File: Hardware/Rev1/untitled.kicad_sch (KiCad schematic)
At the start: 40 parts, among them J4 Female Conn, U3 TPS2596, U4 MCP2542FD-E/SN, U5 AZ1117-5.0, U6 AZ1117-5.0, U7 AZ1117IH-3.3, U9 TPS2596

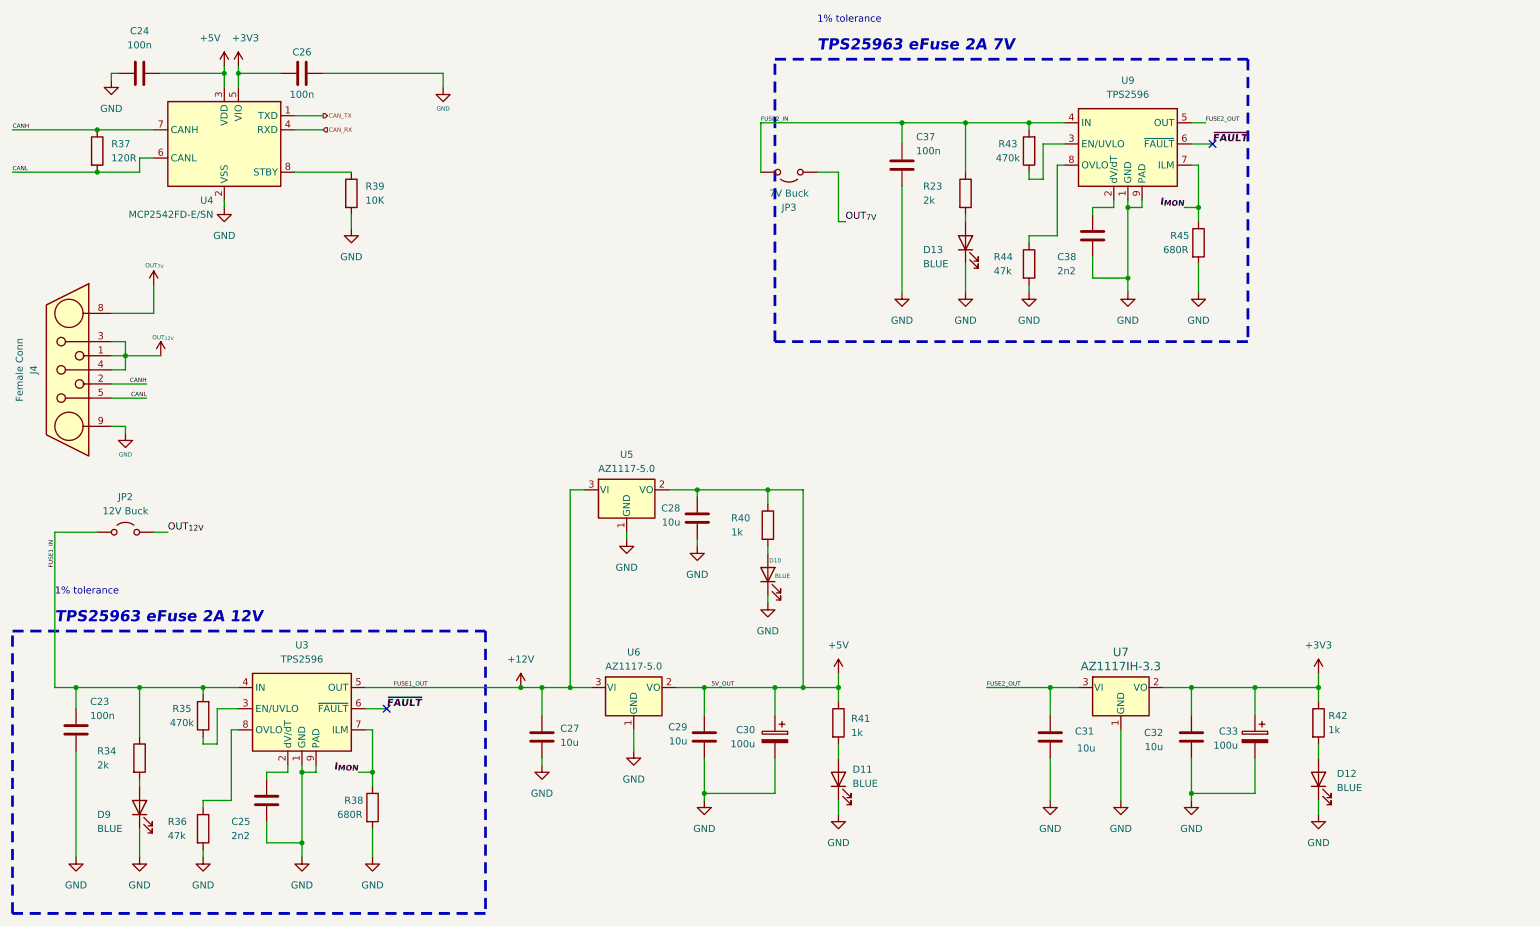
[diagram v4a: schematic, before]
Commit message: updated layout
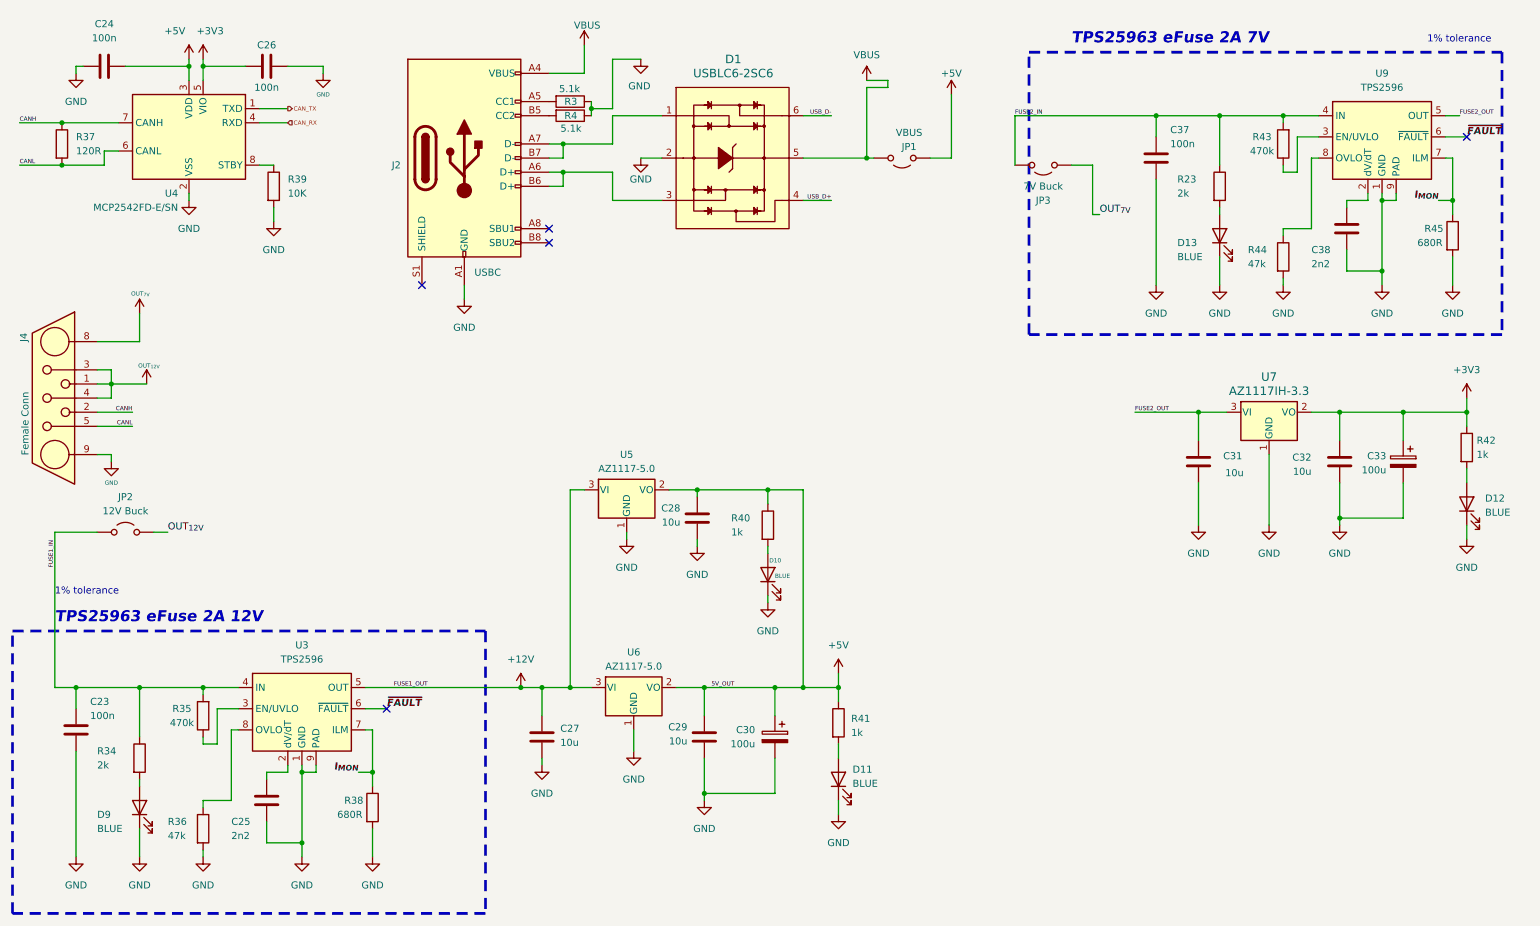
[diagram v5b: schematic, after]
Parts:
- added D1: USBLC6-2SC6, Package_TO_SOT_SMD:TSOT-23-6, symbol dk_TVS-Diodes:USBLC6-2SC6
- added J2: USBC, Connector_USB:USB_C_Receptacle_GCT_USB4105-xx-A_16P_TopMnt_Horizontal, symbol Connector:USB_C_Receptacle_USB2.0_16P
- added JP1: VBUS, ecocad_lib_footprints:J_0603_Triangular, symbol Jumper:Jumper_2_Open
- added R3, R4: 5.1k, Resistor_SMD:R_0603_1608Metric, symbol Device:R
- D10, D11, D12, D13, D9: LCSC# (none) -> C19171394
- R40, R41, R42: LCSC# (none) -> C21190
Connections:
- net +5V: now also JP1.1 (A)
- net GND: now also D1.2, J2.A1 (GND), J2.A12 (GND), J2.B1 (GND), J2.B12 (GND), R3.1, R4.1
- new net: J2.B5 (CC2), R4.2
- new net: J2.A5 (CC1), R3.2
- new net: D1.1, J2.A7 (D-), J2.B7 (D-)
- new net: D1.3, J2.A6 (D+), J2.B6 (D+)
- new net USB_D+: D1.4
- new net USB_D-: D1.6
- new net VBUS: D1.5, J2.A4 (VBUS), J2.A9 (VBUS), J2.B4 (VBUS), J2.B9 (VBUS), JP1.2 (B)
- no-connect marks 2 -> 5
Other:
- moved on the sheet: C24, C26, C31, C32, C33, C37, C38, D12, D13, J4, JP3, R23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
